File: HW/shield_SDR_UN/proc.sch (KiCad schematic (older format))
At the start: 40 parts

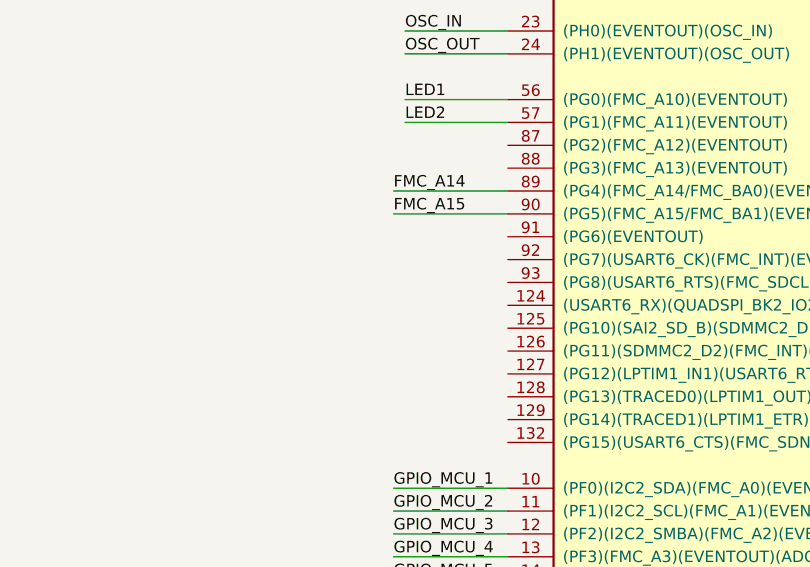
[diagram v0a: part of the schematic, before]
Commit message: OTRA VES FOOTPRINT
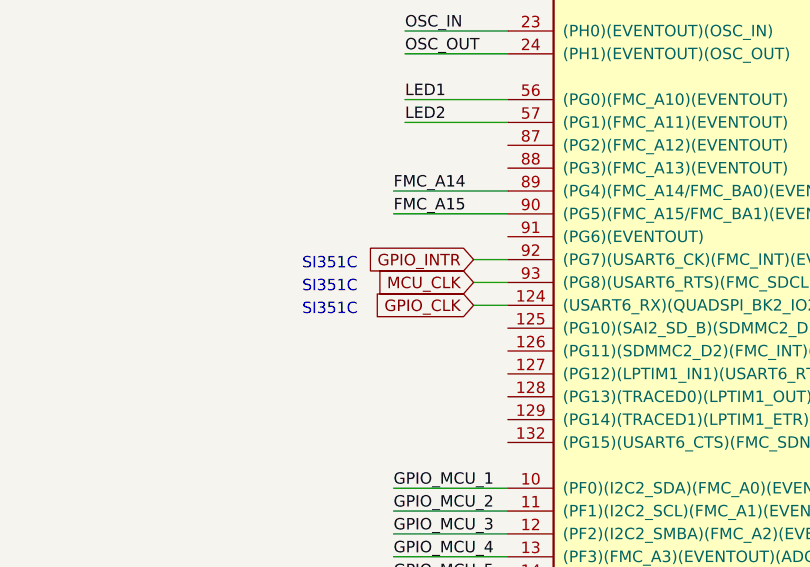
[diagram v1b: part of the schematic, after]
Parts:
- L? (x2): DIGIKEY (none) -> 587-1897-1-ND
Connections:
- net GPIO_CLK: now reaches U?.124 ((USART6_RX)(QUADSPI_BK2_IO2)(SAI2_FS_B)(SDMMC2_D0)(FMC_NE2/FMC_NCE)(EVENTOUT)(PG9))
- net GPIO_INTR: now reaches U?.92 ((PG7)(USART6_CK)(FMC_INT)(EVENTOUT))
- net MCU_CLK: now reaches U?.93 ((PG8)(USART6_RTS)(FMC_SDCLK)(EVENTOUT))
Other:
- note added: "SI351C"
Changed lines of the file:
@@
 F 2 "Inductor_SMD:L_0603_1608Metric_Pad1.05x0.95mm_HandSolder" H 1150 1950 50  0001 C CNN
 F 3 "~" H 1150 1950 50  0001 C CNN
+F 4 "587-1897-1-ND" V 1150 1950 50  0001 C CNN "DIGIKEY"
 	1    1150 1950
 	0    -1   -1   0
@@
 F 2 "Inductor_SMD:L_0603_1608Metric_Pad1.05x0.95mm_HandSolder" H 10250 11000 50  0001 C CNN
 F 3 "~" H 10250 11000 50  0001 C CNN
+F 4 "587-1897-1-ND" H 10250 11000 50  0001 C CNN "DIGIKEY"
 	1    10250 11000
 	1    0    0    -1
@@
 Wire Wire Line
 	2050 5000 2050 5200
-Wire Bus Line
-	7850 12700 7850 12900
-Wire Bus Line
-	5900 13600 5900 13800
-Wire Bus Line
-	9150 12600 9150 13100
-Wire Bus Line
-	5850 12700 5850 13400
-Wire Bus Line
-	11250 13400 11250 14000
-Wire Bus Line
-	13000 12000 13000 13000
-Wire Bus Line
-	11250 11550 11250 13150
 $Comp
 L Device:R R?
@@
 	1    0    0    -1
 $EndComp
+Text GLabel 5900 6250 0    50   Input ~ 0
+GPIO_INTR
+Wire Wire Line
+	5900 6250 6050 6250
+Text Notes 5150 6300 0    50   ~ 0
+SI351C
+Text GLabel 5900 6350 0    50   Input ~ 0
+MCU_CLK
+Wire Wire Line
+	6050 6350 5900 6350
+Text Notes 5150 6400 0    50   ~ 0
+SI351C
+Text GLabel 5900 6450 0    50   Input ~ 0
+GPIO_CLK
+Text Notes 5150 6500 0    50   ~ 0
+SI351C
+Wire Wire Line
+	6050 6450 5900 6450
+Wire Bus Line
+	7850 12700 7850 12900
+Wire Bus Line
+	5900 13600 5900 13800
+Wire Bus Line
+	9150 12600 9150 13100
+Wire Bus Line
+	5850 12700 5850 13400
+Wire Bus Line
+	11250 13400 11250 14000
+Wire Bus Line
+	13000 12000 13000 13000
+Wire Bus Line
+	11250 11550 11250 13150
 $EndSCHEMATC

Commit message: OTRA VES FOOTPRINT_v1
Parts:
- J?: footprint Connector_PinSocket_2.54mm:PinSocket_2x20_P2.54mm_Vertical -> Connector_PinHeader_2.54mm:PinHeader_2x20_P2.54mm_Vertical
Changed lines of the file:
@@
 $Comp
 L Connector_Generic:Conn_02x10_Top_Bottom J?
-U 1 1 5D1F8415
+U 0 0 5D1F8415
 P 2450 12450
 F 0 "J?" H 2500 13067 50  0000 C CNN
 F 1 "Conn_02x10_Top_Bottom" H 2500 12976 50  0000 C CNN
-F 2 "Connector_PinSocket_2.54mm:PinSocket_2x20_P2.54mm_Vertical" H 2450 12450 50  0001 C CNN
+F 2 "Connector_PinHeader_2.54mm:PinHeader_2x20_P2.54mm_Vertical" H 2450 12450 50  0001 C CNN
 F 3 "~" H 2450 12450 50  0001 C CNN
 F 4 "S6106-ND" H 2450 12450 50  0001 C CNN "DIGIKEY"
-	1    2450 12450
+	0    2450 12450
 	1    0    0    -1
 $EndComp

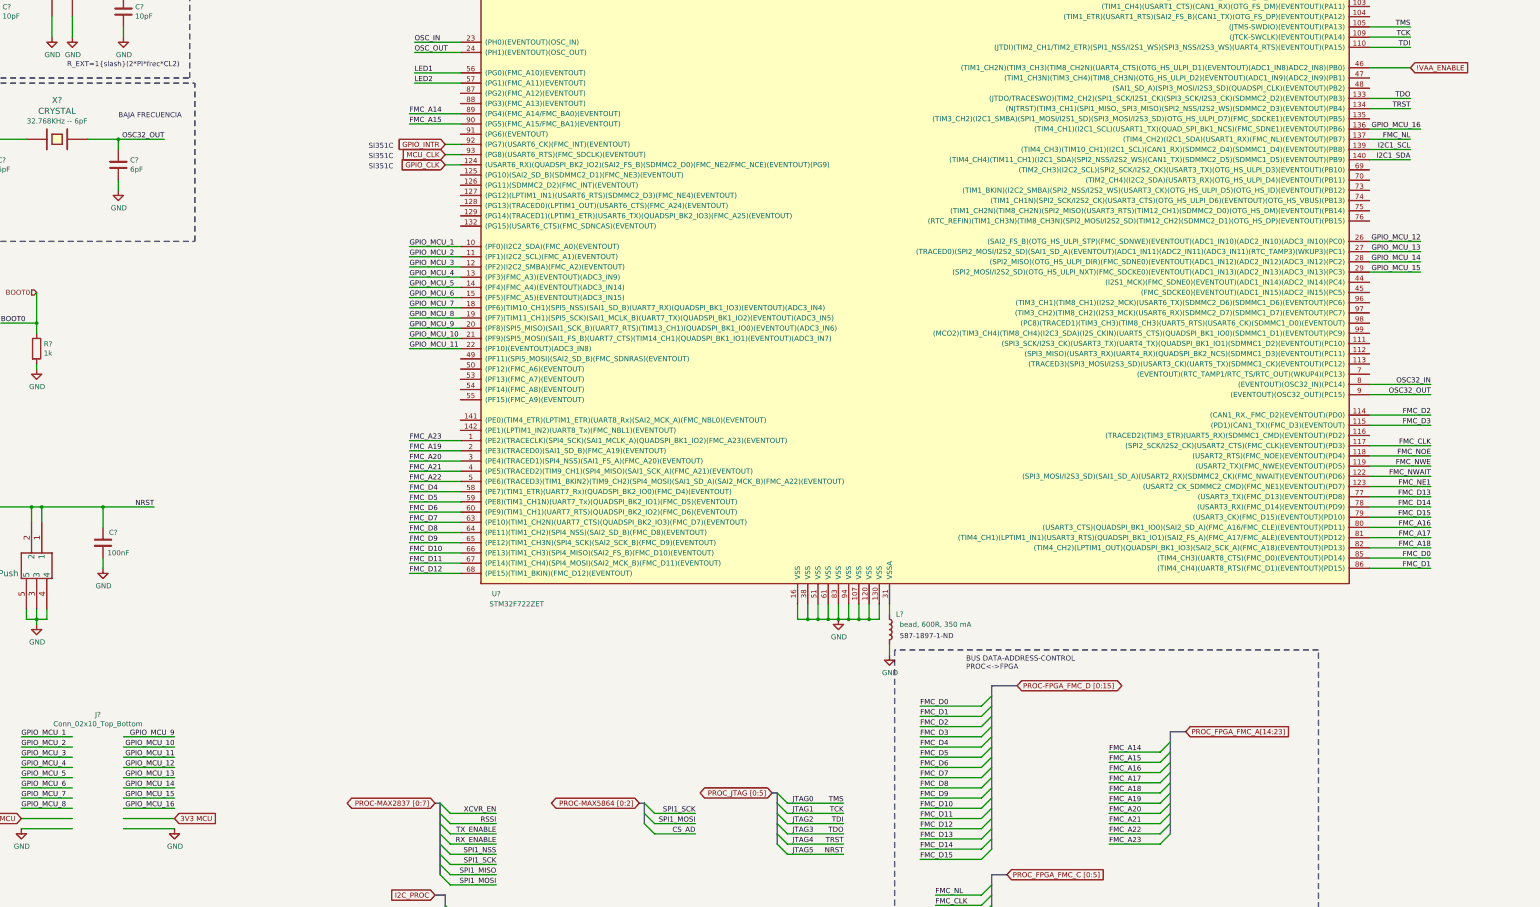
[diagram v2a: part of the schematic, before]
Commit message: RF-Front-end connections
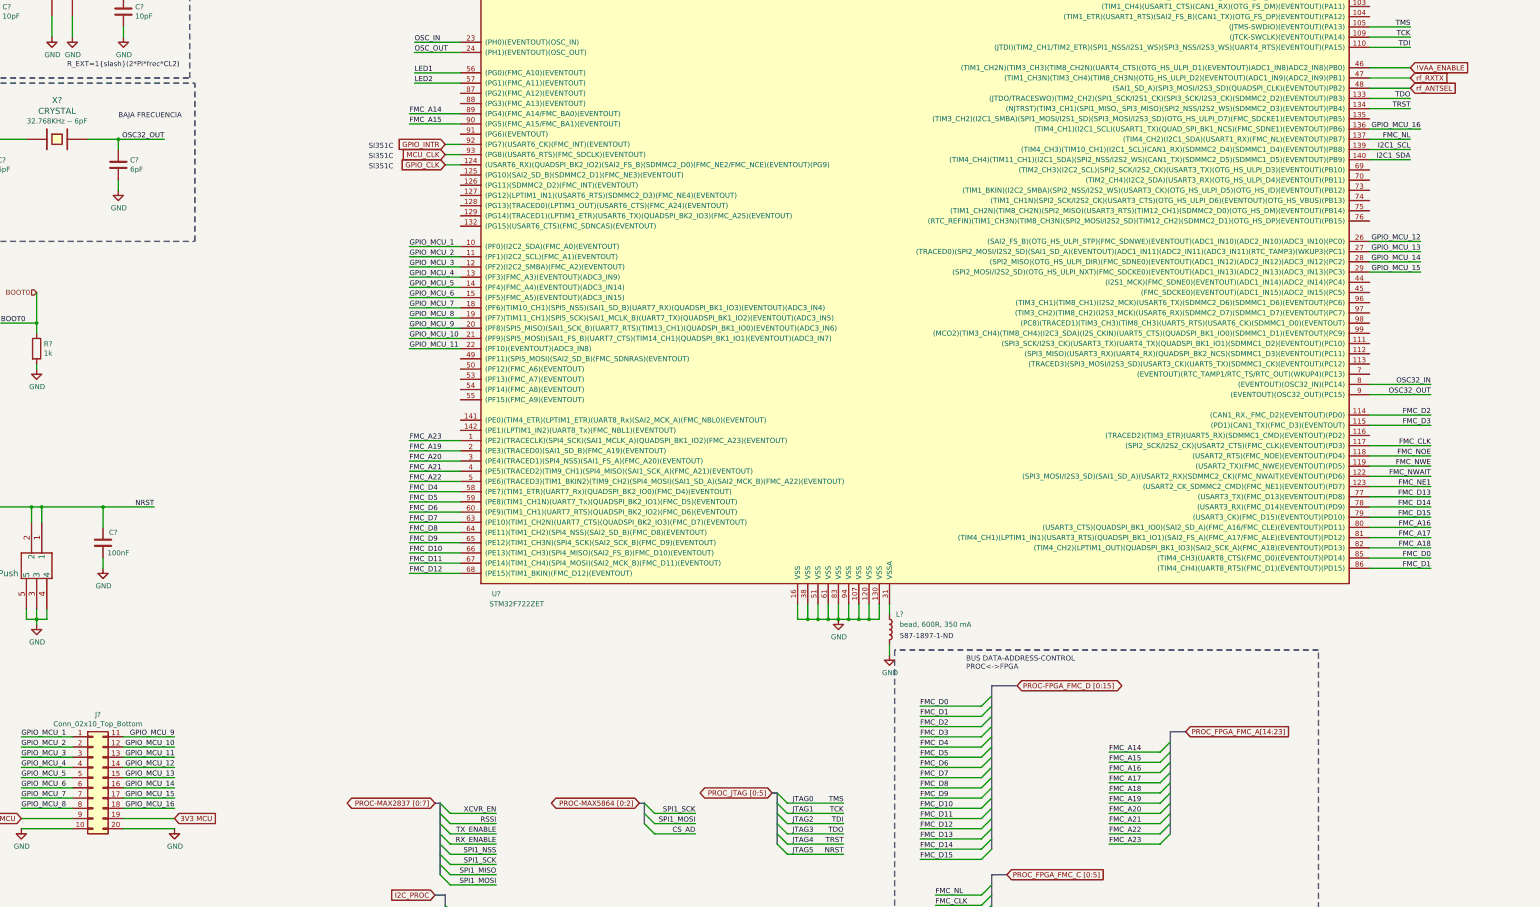
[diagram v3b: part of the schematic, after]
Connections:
- net labels added: rf_ANTSEL, rf_RXTX
- wire segments 332 -> 334
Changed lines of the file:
@@
 $Comp
 L Connector_Generic:Conn_02x10_Top_Bottom J?
-U 0 0 5D1F8415
+U 1 1 5D1F8415
 P 2450 12450
 F 0 "J?" H 2500 13067 50  0000 C CNN
@@
 F 3 "~" H 2450 12450 50  0001 C CNN
 F 4 "S6106-ND" H 2450 12450 50  0001 C CNN "DIGIKEY"
-	0    2450 12450
+	1    2450 12450
 	1    0    0    -1
 $EndComp
@@
 $EndComp
 $Comp
-L power:GND #PWR?
+L power:GND #PWR0216
 U 1 1 5CEAA678
 P 16550 2950
-F 0 "#PWR?" H 16550 2700 50  0001 C CNN
+F 0 "#PWR0216" H 16550 2700 50  0001 C CNN
 F 1 "GND" H 16555 2777 50  0000 C CNN
 F 2 "" H 16550 2950 50  0001 C CNN
@@
 $EndComp
 $Comp
-L power:GND #PWR?
+L power:GND #PWR0217
 U 1 1 5CEAD128
 P 17000 2950
-F 0 "#PWR?" H 17000 2700 50  0001 C CNN
+F 0 "#PWR0217" H 17000 2700 50  0001 C CNN
 F 1 "GND" H 17005 2777 50  0000 C CNN
 F 2 "" H 17000 2950 50  0001 C CNN
@@
 $EndComp
 $Comp
-L power:GND #PWR?
+L power:GND #PWR0218
 U 1 1 5CEA32F9
 P 2250 5200
-F 0 "#PWR?" H 2250 4950 50  0001 C CNN
+F 0 "#PWR0218" H 2250 4950 50  0001 C CNN
 F 1 "GND" H 2255 5027 50  0000 C CNN
 F 2 "" H 2250 5200 50  0001 C CNN
@@
 Wire Wire Line
 	6050 6450 5900 6450
+Text GLabel 15350 5600 2    50   Input ~ 0
+rf_RXTX
+Text GLabel 15350 5700 2    50   Input ~ 0
+rf_ANTSEL
+Wire Wire Line
+	15350 5600 14950 5600
+Wire Wire Line
+	14950 5700 15350 5700
 Wire Bus Line
 	7850 12700 7850 12900
